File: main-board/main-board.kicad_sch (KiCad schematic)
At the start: 0 parts

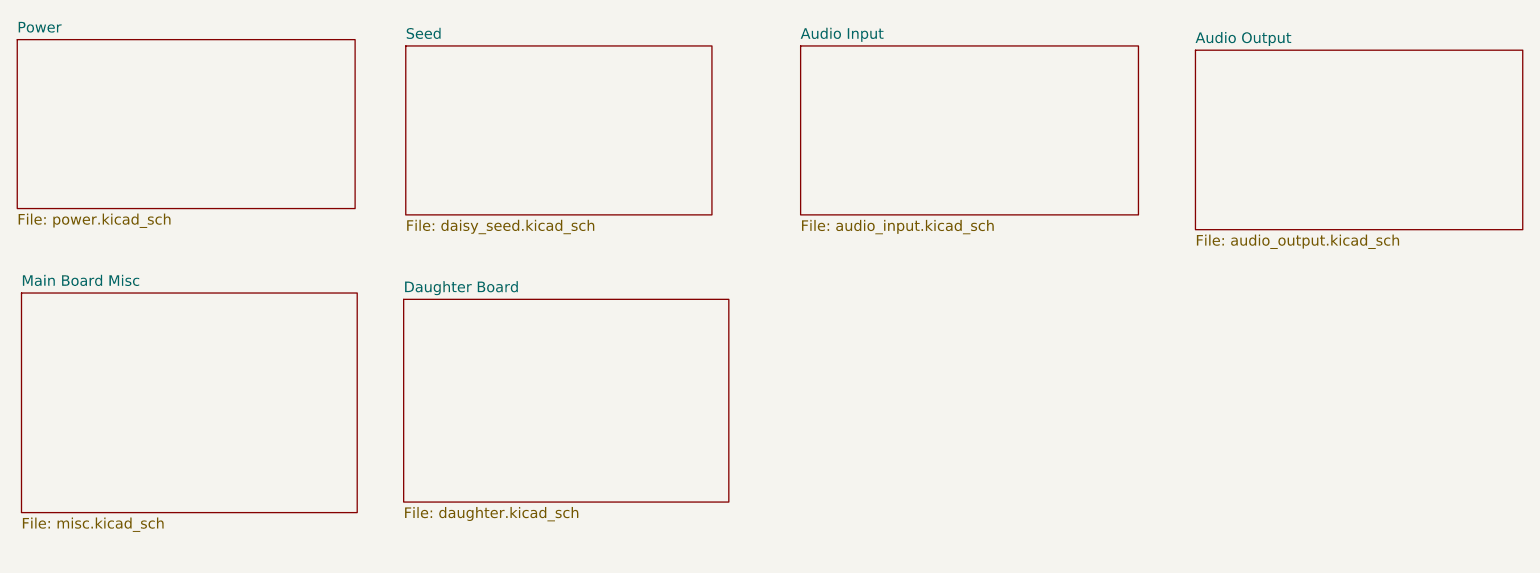
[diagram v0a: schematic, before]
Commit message: wip: working on splitting the daughter board
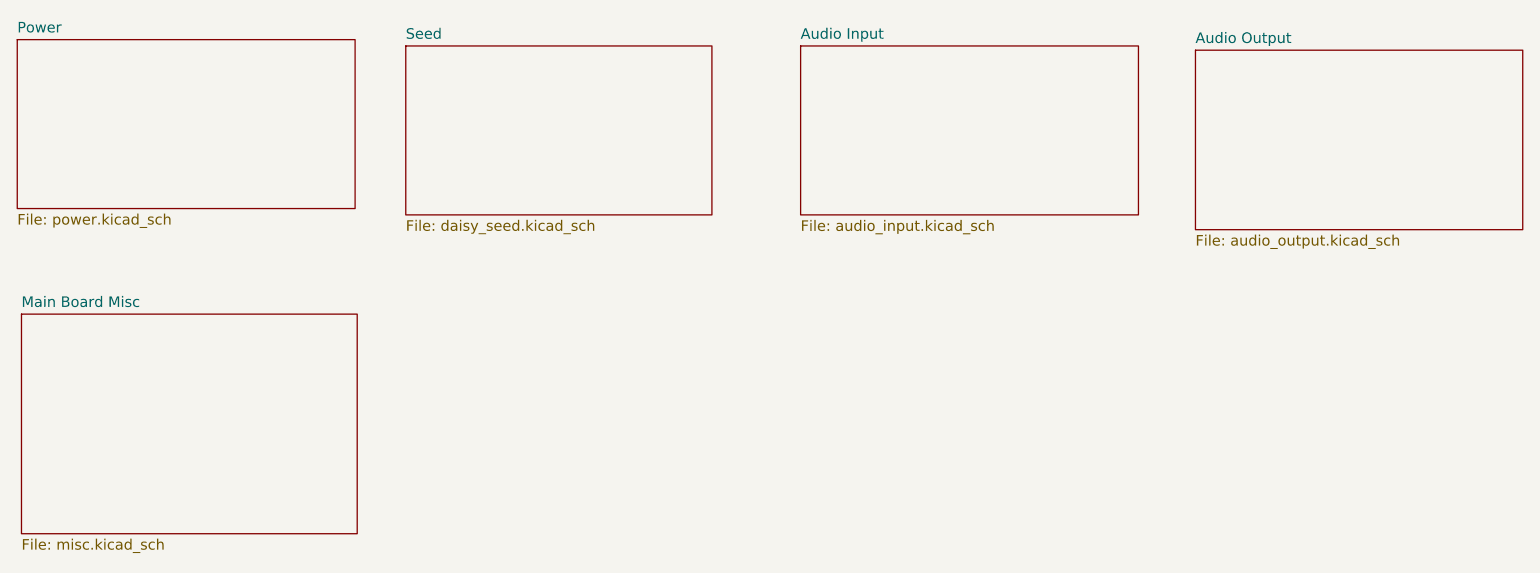
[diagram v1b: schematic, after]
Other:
- removed sheet Daughter Board
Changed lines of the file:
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@@
 		(title "Daisy-Studio")
 		(date "2026-04-17")
-		(rev "2.0")
+		(rev "2c")
 		(company "Rasheed Abdul-Aziz")
 	)
@@
 		)
 		(instances
-			(project "daisy-studio"
+			(project "main-board"
 				(path "/55cca6a8-30da-4c13-b2f2-a01401e2b54c"
 					(page "4")
@@
 		)
 		(instances
-			(project "daisy-studio"
+			(project "main-board"
 				(path "/55cca6a8-30da-4c13-b2f2-a01401e2b54c"
 					(page "3")
-				)
-			)
-		)
-	)
-	(sheet
-		(at 76.962 61.722)
-		(size 39.116 24.384)
-		(exclude_from_sim no)
-		(in_bom yes)
-		(on_board yes)
-		(dnp no)
-		(fields_autoplaced yes)
-		(stroke
-			(width 0.1524)
-			(type solid)
-		)
-		(fill
-			(color 255 229 191 1.0000)
-		)
-		(property "Sheetname" "Daughter Board"
-			(at 76.962 61.0104 0)
-			(effects
-				(font
-					(size 1.27 1.27)
-				)
-				(justify left bottom)
-			)
-		)
-		(property "Sheetfile" "daughter.kicad_sch"
-			(at 76.962 86.6906 0)
-			(effects
-				(font
-					(size 1.27 1.27)
-				)
-				(justify left top)
-			)
-		)
-		(instances
-			(project "daisy-studio"
-				(path "/55cca6a8-30da-4c13-b2f2-a01401e2b54c"
-					(page "7")
 				)
 			)
@@
 		)
 		(instances
-			(project "daisy-studio"
+			(project "main-board"
 				(path "/55cca6a8-30da-4c13-b2f2-a01401e2b54c"
 					(page "2")
@@
 		)
 		(instances
-			(project "daisy-studio"
+			(project "main-board"
 				(path "/55cca6a8-30da-4c13-b2f2-a01401e2b54c"
 					(page "5")
@@
 	)
 	(sheet
-		(at 30.988 60.96)
+		(at 30.988 63.5)
 		(size 40.386 26.416)
 		(exclude_from_sim no)
@@
 		)
 		(property "Sheetname" "Main Board Misc"
-			(at 30.988 60.2484 0)
+			(at 30.988 62.7884 0)
 			(effects
 				(font
@@
 		)
 		(property "Sheetfile" "misc.kicad_sch"
-			(at 30.988 87.9606 0)
-			(effects
-				(font
-					(size 1.27 1.27)
-				)
-				(justify left top)
-			)
-		)
-		(instances
-			(project "daisy-studio"
+			(at 30.988 90.5006 0)
+			(effects
+				(font
+					(size 1.27 1.27)
+				)
+				(justify left top)
+			)
+		)
+		(instances
+			(project "main-board"
 				(path "/55cca6a8-30da-4c13-b2f2-a01401e2b54c"
 					(page "6")
